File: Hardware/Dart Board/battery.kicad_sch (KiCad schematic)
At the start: 2 parts, among them J3 Conn_01x02_Pin, SW2 SW_SPST

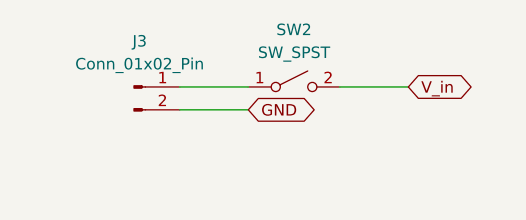
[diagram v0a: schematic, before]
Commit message: Assigned Footprints and added to PCB editor
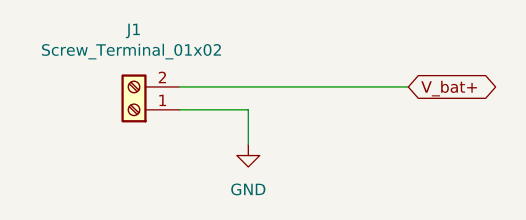
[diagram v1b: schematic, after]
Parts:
- removed J3: Conn_01x02_Pin, symbol Connector:Conn_01x02_Pin
- removed SW2: SW_SPST, symbol Switch:SW_SPST
- added J1: Screw_Terminal_01x02, TerminalBlock:TerminalBlock_MaiXu_MX126-5.0-02P_1x02_P5.00mm, symbol Connector:Screw_Terminal_01x02
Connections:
- net GND: now also J1.1 (Pin_1)
- new net V_bat+: J1.2 (Pin_2)
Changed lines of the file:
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@@
 	(wire
 		(pts
-			(xy 107.95 78.74) (xy 115.57 78.74)
+			(xy 115.57 81.28) (xy 115.57 85.09)
+		)
+		(stroke
+			(width 0)
+			(type default)
+		)
+	)
+	(wire
+		(pts
+			(xy 107.95 78.74) (xy 133.35 78.74)
 		)
 		(stroke
@@
 		)
 	)
-	(wire
-		(pts
-			(xy 125.73 78.74) (xy 133.35 78.74)
-		)
-		(stroke
-			(width 0)
-			(type default)
-		)
-	)
-	(global_label "GND"
-		(shape bidirectional)
-		(at 115.57 81.28 0)
-		(fields_autoplaced yes)
-		(effects
-			(font
-				(size 1.27 1.27)
-			)
-			(justify left)
-		)
-		(property "Intersheetrefs" "${INTERSHEET_REFS}"
-			(at 123.537 81.28 0)
-			(effects
-				(font
-					(size 1.27 1.27)
-				)
-				(justify left)
-				(hide yes)
-			)
-		)
-	)
-	(global_label "V_in"
+	(global_label "V_bat+"
 		(shape bidirectional)
 		(at 133.35 78.74 0)
@@
 		)
 		(property "Intersheetrefs" "${INTERSHEET_REFS}"
-			(at 141.2565 78.74 0)
+			(at 144.0988 78.74 0)
 			(effects
 				(font
@@
 	)
 	(symbol
-		(lib_id "Switch:SW_SPST")
-		(at 120.65 78.74 0)
+		(lib_id "power:GND")
+		(at 115.57 85.09 0)
 		(unit 1)
 		(exclude_from_sim no)
@@
 		(dnp no)
 		(fields_autoplaced yes)
-		(property "Reference" "SW2"
-			(at 120.65 72.39 0)
+		(property "Reference" "#PWR025"
+			(at 115.57 91.44 0)
 			(effects
 				(font
 					(size 1.27 1.27)
 				)
+				(hide yes)
 			)
 		)
-		(property "Value" "SW_SPST"
-			(at 120.65 74.93 0)
+		(property "Value" "GND"
+			(at 115.57 90.17 0)
 			(effects
 				(font
@@
 		)
 		(property "Footprint" ""
-			(at 120.65 78.74 0)
+			(at 115.57 85.09 0)
+			(effects
+				(font
+					(size 1.27 1.27)
+				)
+				(hide yes)
+			)
+		)
+		(property "Datasheet" ""
+			(at 115.57 85.09 0)
+			(effects
+				(font
+					(size 1.27 1.27)
+				)
+				(hide yes)
+			)
+		)
+		(property "Description" "Power symbol creates a global label with name \"GND\" , ground"
+			(at 115.57 85.09 0)
+			(effects
+				(font
+					(size 1.27 1.27)
+				)
+				(hide yes)
+			)
+		)
+		(pin "1"
+		)
+		(instances
+			(project ""
+				(path "/1d6d0dd6-dd3e-4fbe-b34b-7dc303157c7e/1d6b9460-2cc3-44ee-8d8e-92df70587700"
+					(reference "#PWR025")
+					(unit 1)
+				)
+			)
+		)
+	)
+	(symbol
+		(lib_id "Connector:Screw_Terminal_01x02")
+		(at 102.87 81.28 180)
+		(unit 1)
+		(exclude_from_sim no)
+		(in_bom yes)
+		(on_board yes)
+		(dnp no)
+		(property "Reference" "J1"
+			(at 102.87 72.39 0)
+			(effects
+				(font
+					(size 1.27 1.27)
+				)
+			)
+		)
+		(property "Value" "Screw_Terminal_01x02"
+			(at 102.616 74.676 0)
+			(effects
+				(font
+					(size 1.27 1.27)
+				)
+			)
+		)
+		(property "Footprint" "TerminalBlock:TerminalBlock_MaiXu_MX126-5.0-02P_1x02_P5.00mm"
+			(at 102.87 81.28 0)
 			(effects
 				(font
@@
 		)
 		(property "Datasheet" "~"
-			(at 120.65 78.74 0)
+			(at 102.87 81.28 0)
 			(effects
 				(font
@@
 			)
 		)
-		(property "Description" "Single Pole Single Throw (SPST) switch"
-			(at 120.65 78.74 0)
-			(effects
-				(font
-					(size 1.27 1.27)
-				)
-				(hide yes)
-			)
-		)
-		(pin "2"
-		)
-		(pin "1"
-		)
-		(instances
-			(project ""
-				(path "/1d6d0dd6-dd3e-4fbe-b34b-7dc303157c7e/1d6b9460-2cc3-44ee-8d8e-92df70587700"
-					(reference "SW2")
-					(unit 1)
-				)
-			)
-		)
-	)
-	(symbol
-		(lib_id "Connector:Conn_01x02_Pin")
-		(at 102.87 78.74 0)
-		(unit 1)
-		(exclude_from_sim no)
-		(in_bom yes)
-		(on_board yes)
-		(dnp no)
-		(fields_autoplaced yes)
-		(property "Reference" "J3"
-			(at 103.505 73.66 0)
-			(effects
-				(font
-					(size 1.27 1.27)
-				)
-			)
-		)
-		(property "Value" "Conn_01x02_Pin"
-			(at 103.505 76.2 0)
-			(effects
-				(font
-					(size 1.27 1.27)
-				)
-			)
-		)
-		(property "Footprint" ""
-			(at 102.87 78.74 0)
-			(effects
-				(font
-					(size 1.27 1.27)
-				)
-				(hide yes)
-			)
-		)
-		(property "Datasheet" "~"
-			(at 102.87 78.74 0)
-			(effects
-				(font
-					(size 1.27 1.27)
-				)
-				(hide yes)
-			)
-		)
-		(property "Description" "Generic connector, single row, 01x02, script generated"
-			(at 102.87 78.74 0)
+		(property "Description" "Generic screw terminal, single row, 01x02, script generated (kicad-library-utils/schlib/autogen/connector/)"
+			(at 102.87 81.28 0)
 			(effects
 				(font
@@
 			(project "Dart Board"
 				(path "/1d6d0dd6-dd3e-4fbe-b34b-7dc303157c7e/1d6b9460-2cc3-44ee-8d8e-92df70587700"
-					(reference "J3")
+					(reference "J1")
 					(unit 1)
 				)
